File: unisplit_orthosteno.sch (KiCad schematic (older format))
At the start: 57 parts, among them U1 ProMicro

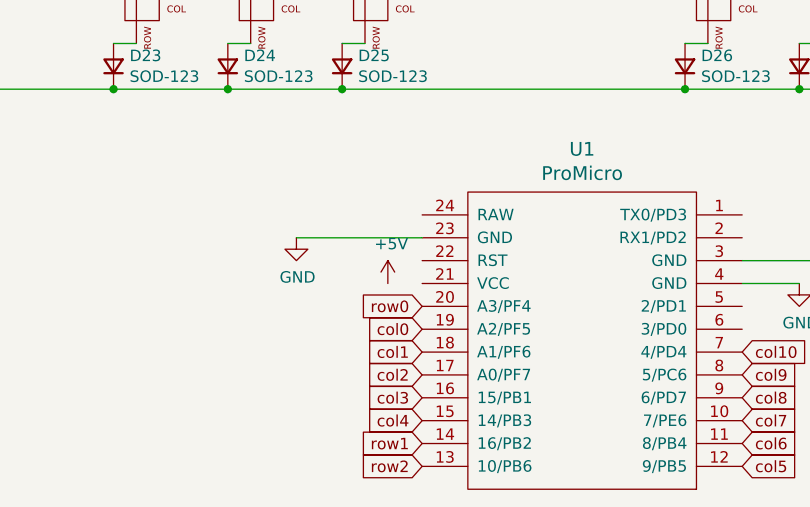
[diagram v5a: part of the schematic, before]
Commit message: update case files, now the cases should be okay, case may be a bit tight so scaling up like 0.001 percent might help when 3d printing it
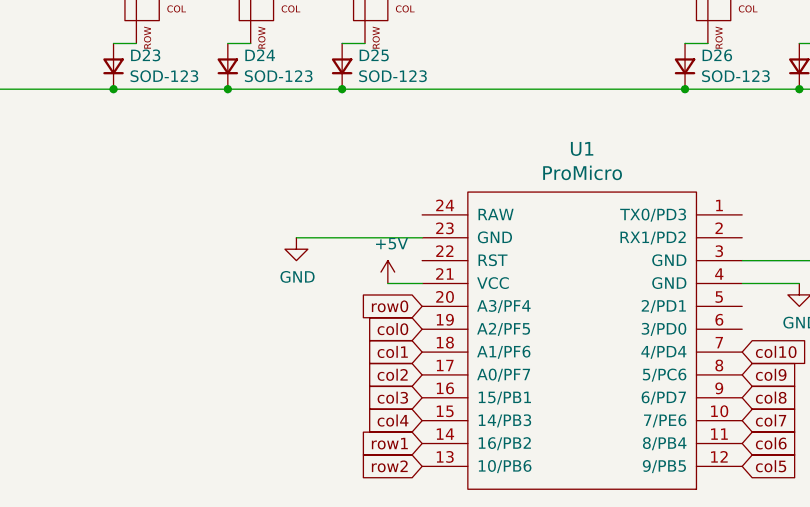
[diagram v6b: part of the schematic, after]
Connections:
- net +5V: now also U1.21 (VCC)
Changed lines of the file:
@@
 	0    -1   -1   0
 $EndComp
+Wire Wire Line
+	4650 4550 4800 4550
 $EndSCHEMATC
